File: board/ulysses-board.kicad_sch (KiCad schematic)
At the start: 1 part, among them J1 GPIO

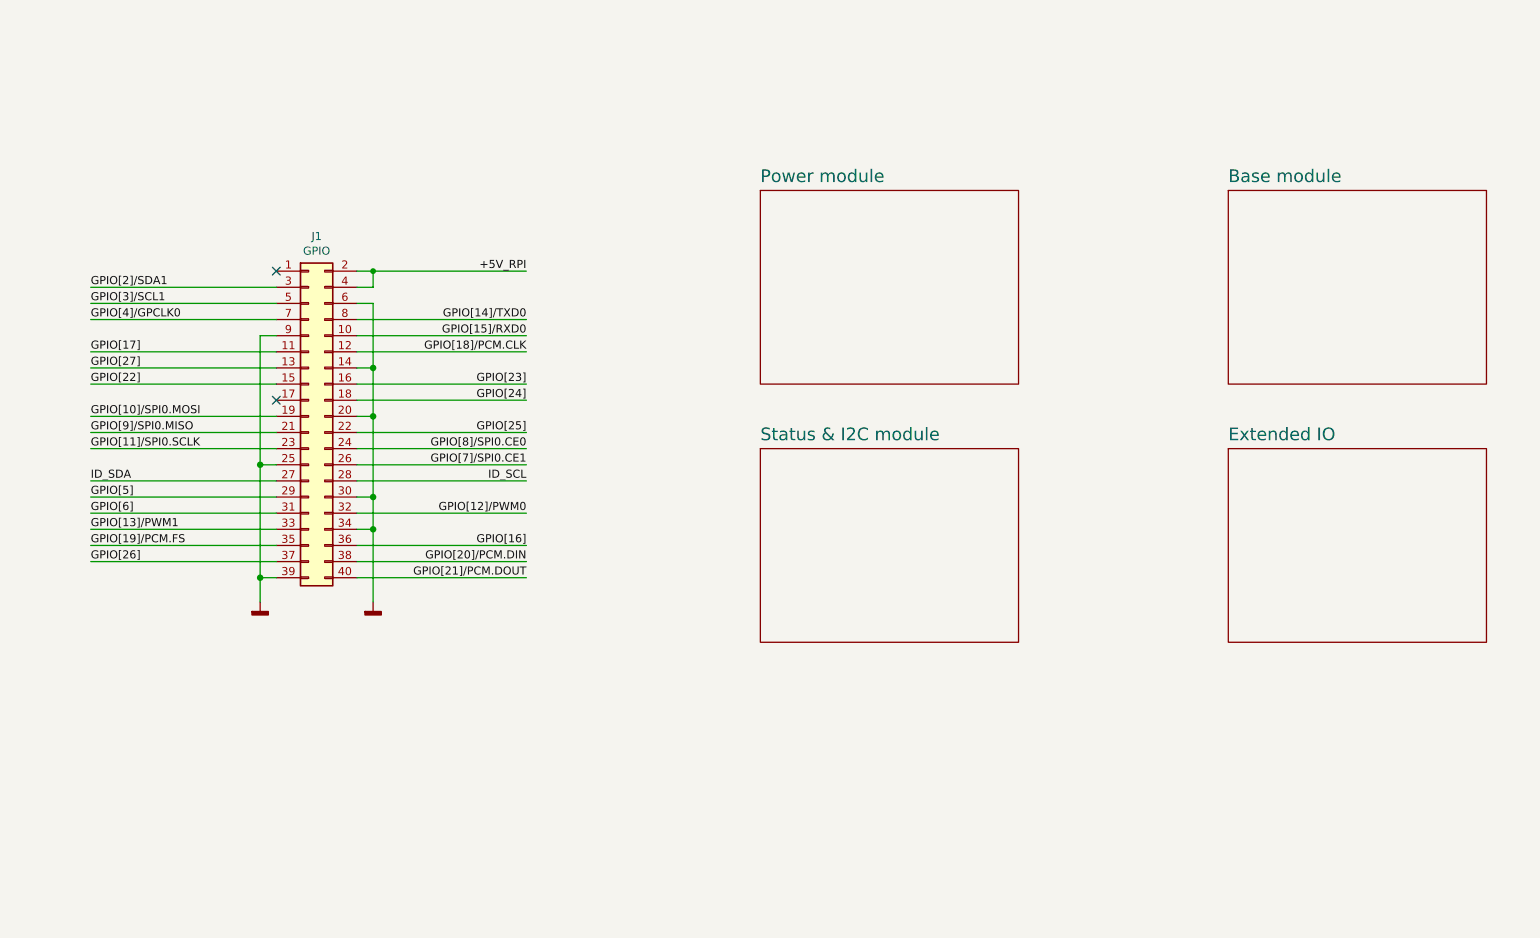
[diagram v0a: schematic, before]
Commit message: Re-structure schematics and improve safety.
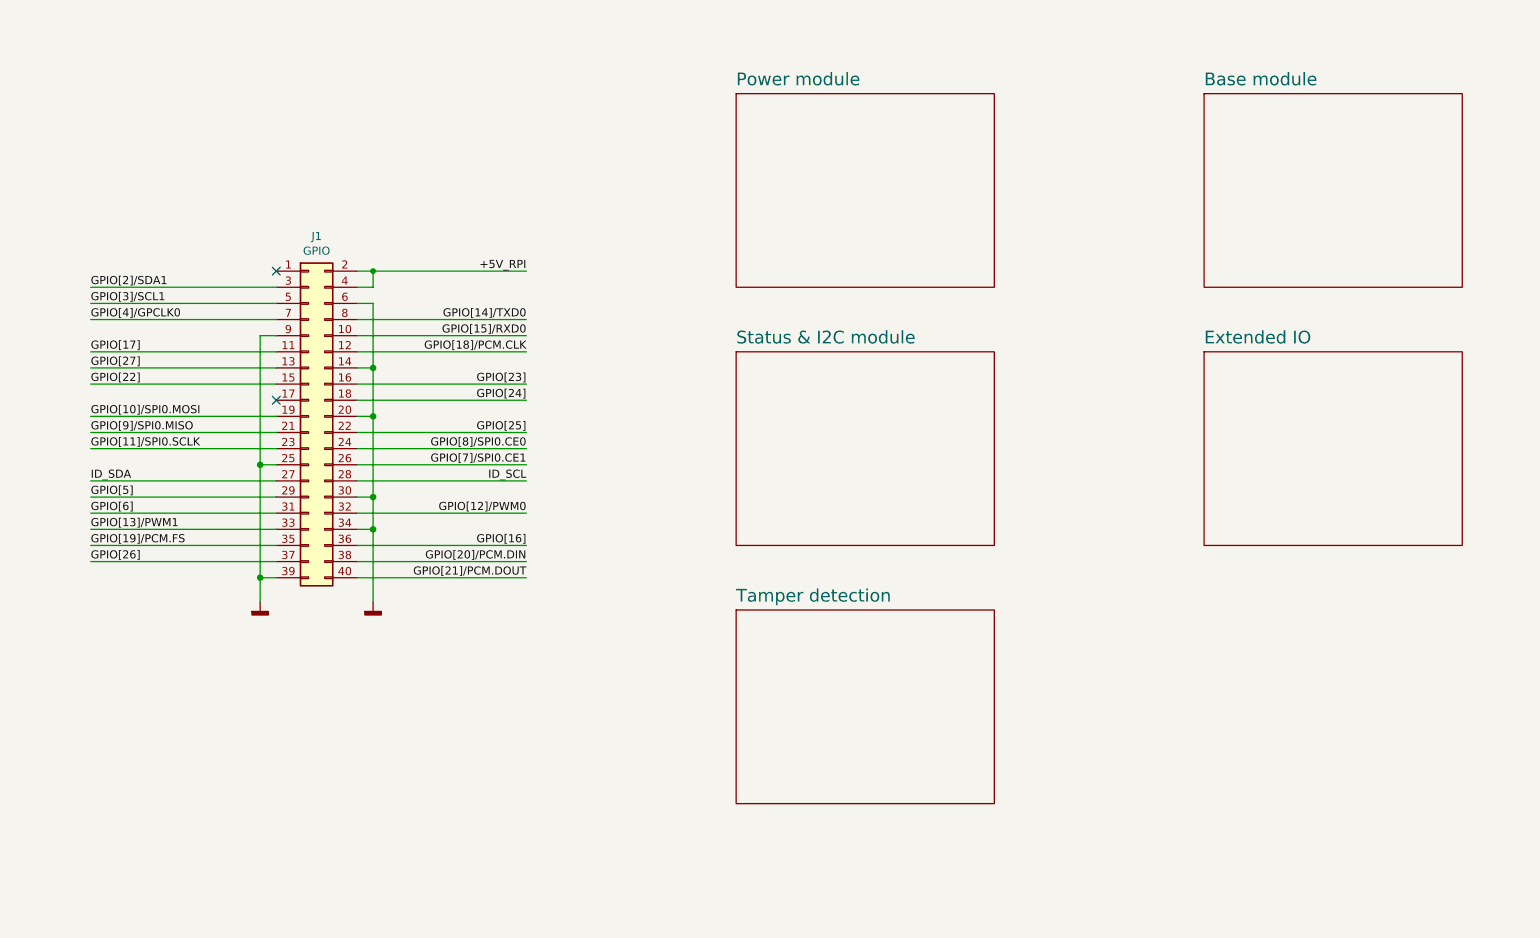
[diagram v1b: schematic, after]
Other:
- added sheet Tamper detection (tamper_detect.kicad_sch)
- sheet Status & I2C module: file extended_io.kicad_sch -> status_i2c.kicad_sch

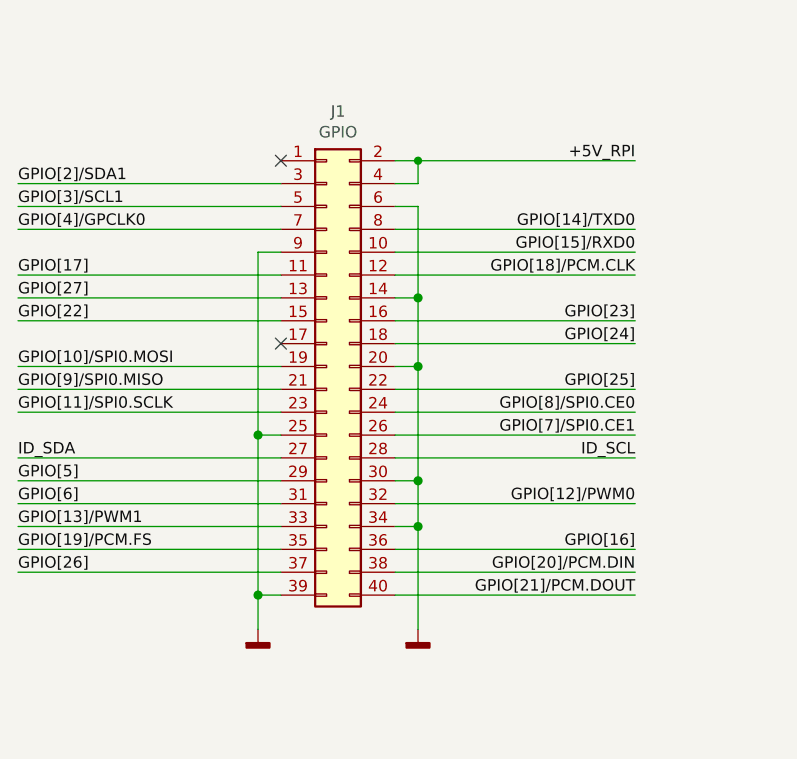
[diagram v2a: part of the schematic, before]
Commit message: Change net descriptors.
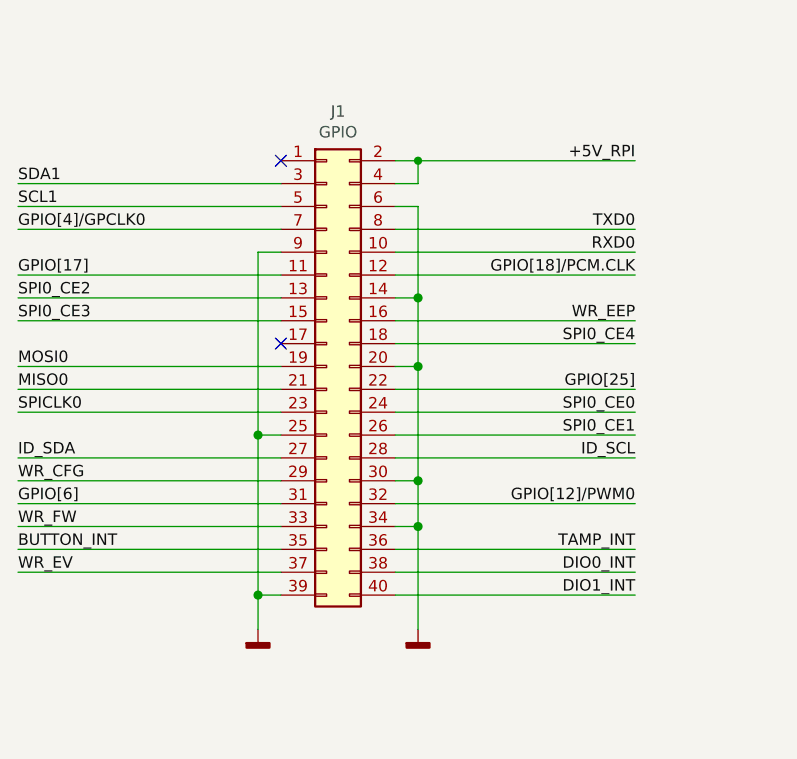
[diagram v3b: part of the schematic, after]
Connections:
- net GPIO[10]/SPI0.MOSI renamed MOSI0
- net GPIO[11]/SPI0.SCLK renamed SPICLK0
- net GPIO[13]/PWM1 renamed WR_FW
- net GPIO[14]/TXD0 renamed TXD0
- net GPIO[15]/RXD0 renamed RXD0
- net GPIO[16] renamed TAMP_INT
- net GPIO[19]/PCM.FS renamed BUTTON_INT
- net GPIO[20]/PCM.DIN renamed DIO0_INT
- net GPIO[21]/PCM.DOUT renamed DIO1_INT
- net GPIO[22] renamed SPI0_CE3
- net GPIO[23] renamed WR_EEP
- net GPIO[24] renamed SPI0_CE4
- net GPIO[26] renamed WR_EV
- net GPIO[27] renamed SPI0_CE2
- net GPIO[2]/SDA1 renamed SDA1
- net GPIO[3]/SCL1 renamed SCL1
- net GPIO[5] renamed WR_CFG
- net GPIO[7]/SPI0.CE1 renamed SPI0_CE1
- net GPIO[8]/SPI0.CE0 renamed SPI0_CE0
- net GPIO[9]/SPI0.MISO renamed MISO0
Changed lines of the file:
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@@
     (effects (font (size 1.27 1.27)) (justify right bottom))
   )
-  (label "GPIO[5]" (at 36.83 93.98 0)
+  (label "WR_CFG" (at 36.83 93.98 0)
     (effects (font (size 1.27 1.27)) (justify left bottom))
   )
-  (label "GPIO[21]{slash}PCM.DOUT" (at 105.41 106.68 180)
+  (label "DIO1_INT" (at 105.41 106.68 180)
     (effects (font (size 1.27 1.27)) (justify right bottom))
   )
-  (label "GPIO[19]{slash}PCM.FS" (at 36.83 101.6 0)
+  (label "MOSI0" (at 36.83 81.28 0)
     (effects (font (size 1.27 1.27)) (justify left bottom))
   )
-  (label "GPIO[10]{slash}SPI0.MOSI" (at 36.83 81.28 0)
+  (label "MISO0" (at 36.83 83.82 0)
     (effects (font (size 1.27 1.27)) (justify left bottom))
   )
-  (label "GPIO[9]{slash}SPI0.MISO" (at 36.83 83.82 0)
-    (effects (font (size 1.27 1.27)) (justify left bottom))
-  )
-  (label "GPIO[23]" (at 105.41 76.2 180)
+  (label "WR_EEP" (at 105.41 76.2 180)
     (effects (font (size 1.27 1.27)) (justify right bottom))
   )
@@
     (effects (font (size 1.27 1.27)) (justify left bottom))
   )
-  (label "GPIO[27]" (at 36.83 73.66 0)
+  (label "SPI0_CE2" (at 36.83 73.66 0)
     (effects (font (size 1.27 1.27)) (justify left bottom))
   )
-  (label "GPIO[26]" (at 36.83 104.14 0)
+  (label "WR_EV" (at 36.83 104.14 0)
     (effects (font (size 1.27 1.27)) (justify left bottom))
   )
-  (label "GPIO[14]{slash}TXD0" (at 105.41 66.04 180)
+  (label "TXD0" (at 105.41 66.04 180)
     (effects (font (size 1.27 1.27)) (justify right bottom))
   )
-  (label "GPIO[8]{slash}SPI0.CE0" (at 105.41 86.36 180)
+  (label "SPI0_CE0" (at 105.41 86.36 180)
     (effects (font (size 1.27 1.27)) (justify right bottom))
   )
-  (label "GPIO[15]{slash}RXD0" (at 105.41 68.58 180)
+  (label "RXD0" (at 105.41 68.58 180)
     (effects (font (size 1.27 1.27)) (justify right bottom))
   )
-  (label "GPIO[16]" (at 105.41 101.6 180)
-    (effects (font (size 1.27 1.27)) (justify right bottom))
-  )
-  (label "GPIO[22]" (at 36.83 76.2 0)
+  (label "SPI0_CE3" (at 36.83 76.2 0)
     (effects (font (size 1.27 1.27)) (justify left bottom))
   )
-  (label "GPIO[2]{slash}SDA1" (at 36.83 60.96 0)
+  (label "SDA1" (at 36.83 60.96 0)
     (effects (font (size 1.27 1.27)) (justify left bottom))
   )
@@
     (effects (font (size 1.27 1.27)) (justify right bottom))
   )
-  (label "GPIO[3]{slash}SCL1" (at 36.83 63.5 0)
+  (label "SCL1" (at 36.83 63.5 0)
     (effects (font (size 1.27 1.27)) (justify left bottom))
   )
@@
     (effects (font (size 1.27 1.27)) (justify right bottom))
   )
-  (label "GPIO[13]{slash}PWM1" (at 36.83 99.06 0)
+  (label "WR_FW" (at 36.83 99.06 0)
     (effects (font (size 1.27 1.27)) (justify left bottom))
   )
-  (label "GPIO[20]{slash}PCM.DIN" (at 105.41 104.14 180)
+  (label "DIO0_INT" (at 105.41 104.14 180)
     (effects (font (size 1.27 1.27)) (justify right bottom))
   )
-  (label "GPIO[24]" (at 105.41 78.74 180)
+  (label "SPI0_CE4" (at 105.41 78.74 180)
     (effects (font (size 1.27 1.27)) (justify right bottom))
   )
-  (label "GPIO[7]{slash}SPI0.CE1" (at 105.41 88.9 180)
+  (label "SPI0_CE1" (at 105.41 88.9 180)
     (effects (font (size 1.27 1.27)) (justify right bottom))
   )
-  (label "GPIO[11]{slash}SPI0.SCLK" (at 36.83 86.36 0)
+  (label "BUTTON_INT" (at 36.83 101.6 0)
     (effects (font (size 1.27 1.27)) (justify left bottom))
   )
+  (label "TAMP_INT" (at 105.41 101.6 180)
+    (effects (font (size 1.27 1.27)) (justify right bottom))
+  )
+  (label "SPICLK0" (at 36.83 86.36 0)
+    (effects (font (size 1.27 1.27)) (justify left bottom))
+  )
